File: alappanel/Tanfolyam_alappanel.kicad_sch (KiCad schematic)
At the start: 22 parts, among them J1 Connector, J2 Connector

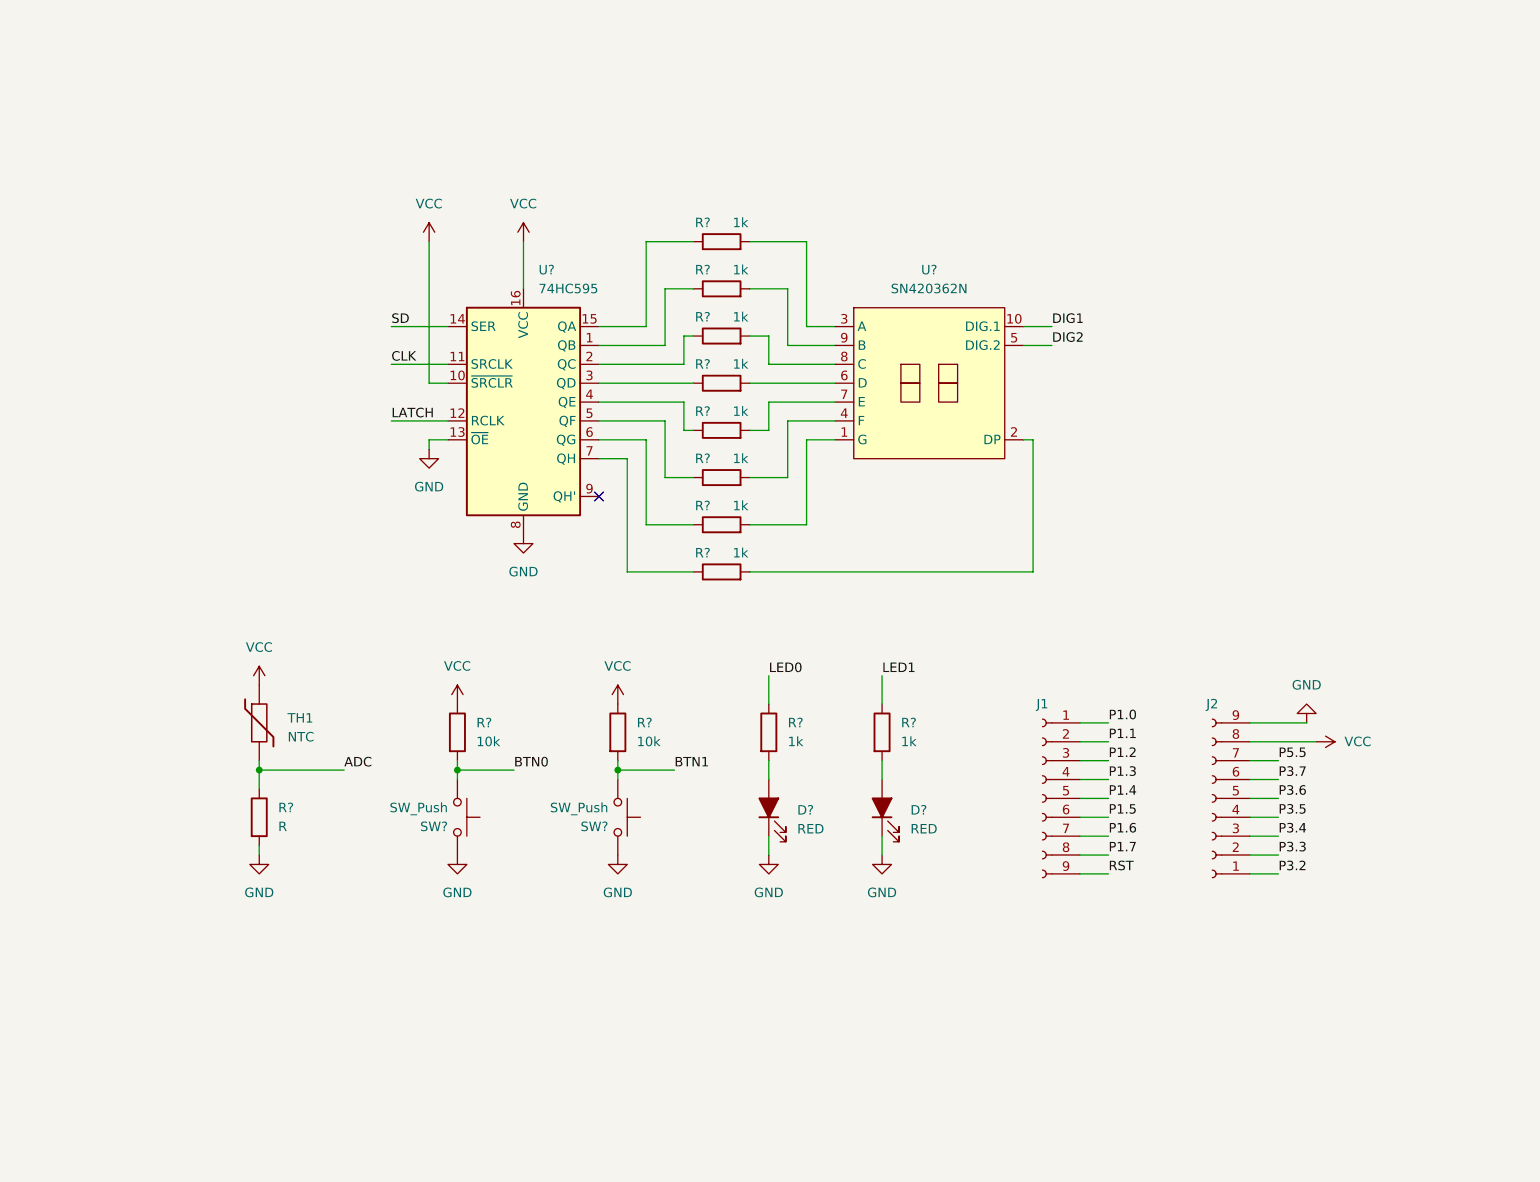
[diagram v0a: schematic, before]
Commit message: Add single sided base board
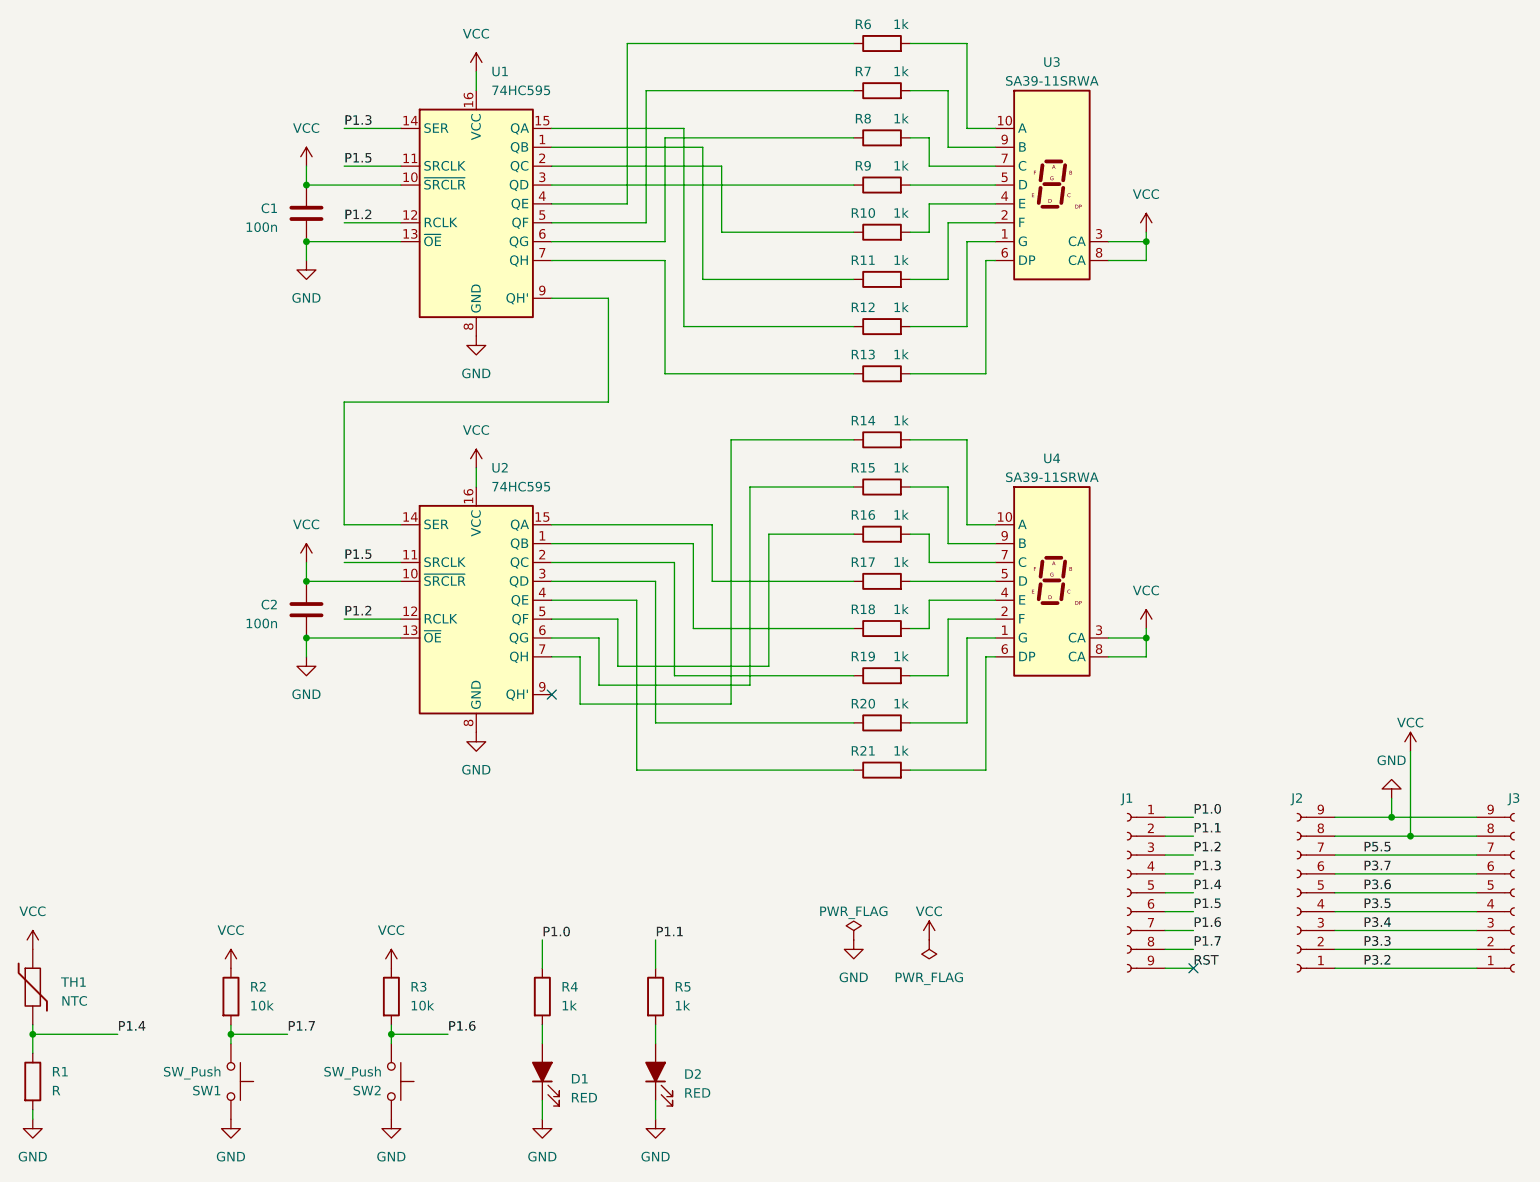
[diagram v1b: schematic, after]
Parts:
- removed R? (x7): 1k, symbol Device:R
- removed U?: SN420362N, sem-tanfolyam:SN420362N, symbol sem-tanfolyam:SN420362N
- removed U?: 74HC595, symbol 74xx:74HC595
- added C1, C2: 100n, Capacitor_SMD:C_0805_2012Metric_Pad1.18x1.45mm_HandSolder, symbol Device:C
- added J3: Connector, Connector_PinHeader_2.54mm:PinHeader_1x09_P2.54mm_Vertical, symbol Connector:Conn_01x09_Socket
- added R10, R11, R12, R13, R14, R15, R16, R17, R18, R19, R20, R21, R7, R8, R9: 1k, Resistor_SMD:R_0805_2012Metric_Pad1.20x1.40mm_HandSolder, symbol Device:R
- added U1, U2: 74HC595, Package_SO:SOIC-16_3.9x9.9mm_P1.27mm, symbol 74xx:74HC595
- added U3, U4: SA39-11SRWA, Display_7Segment:Sx39-1xxxxx, symbol Display_Character:SA39-11SRWA
- D1, D2: renamed from D?; footprint (none) -> LED_THT:LED_D5.0mm
- J1, J2: footprint (none) -> Connector_PinSocket_2.54mm:PinSocket_1x09_P2.54mm_Vertical
- R1, R2, R3, R4, R5, R6: renamed from R?; footprint (none) -> Resistor_SMD:R_0805_2012Metric_Pad1.20x1.40mm_HandSolder
- SW1, SW2: renamed from SW?; footprint (none) -> Button_Switch_THT:SW_PUSH_6mm
- TH1: footprint (none) -> Connector_PinHeader_2.54mm:PinHeader_1x02_P2.54mm_Vertical
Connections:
- net ADC is gone; now on net P1.4: R1.1, TH1.2
- net BTN0 is gone; now on net P1.7: R2.2, SW1.1
- net BTN1 is gone; now on net P1.6: R3.2, SW2.1
- net LED0 is gone; now on net P1.0: R4.1
- net LED1 is gone; now on net P1.1: R5.1
- net GND: now also C1.2, C2.2, J3.9 (Pin_9), U1.13 (~{OE}), U1.8 (GND), U2.13 (~{OE}), U2.8 (GND)
- net P1.2: now also U1.12 (RCLK), U2.12 (RCLK)
- net P1.3: now also U1.14 (SER)
- net P1.5: now also U1.11 (SRCLK), U2.11 (SRCLK)
- net P3.2: now also J3.1 (Pin_1)
- net P3.3: now also J3.2 (Pin_2)
- net P3.4: now also J3.3 (Pin_3)
- net P3.5: now also J3.4 (Pin_4)
- net P3.6: now also J3.5 (Pin_5)
- net P3.7: now also J3.6 (Pin_6)
- net P5.5: now also J3.7 (Pin_7)
- net VCC: now also C1.1, C2.1, J3.8 (Pin_8), U1.10 (~{SRCLR}), U1.16 (VCC), U2.10 (~{SRCLR}), U2.16 (VCC), U3.3 (CA), U3.8 (CA), U4.3 (CA), U4.8 (CA)
- net at R6.2: now also U3.10 (A)
- net at R6.1: now also U1.4 (QE)
- new net: R12.2, U3.1 (G)
- new net: R11.2, U3.2 (F)
- new net: R10.2, U3.4 (E)
- new net: R9.2, U3.5 (D)
- new net: R13.2, U3.6 (DP)
- new net: R8.2, U3.7 (C)
- new net: R7.2, U3.9 (B)
- new net: R20.2, U4.1 (G)
- new net: R14.2, U4.10 (A)
- new net: R19.2, U4.2 (F)
- new net: R18.2, U4.4 (E)
- new net: R17.2, U4.5 (D)
- new net: R21.2, U4.6 (DP)
- new net: R16.2, U4.7 (C)
- new net: R15.2, U4.9 (B)
- new net: R16.1, U2.5 (QF)
- new net: R12.1, U1.15 (QA)
- new net: R14.1, U2.7 (QH)
- new net: R8.1, U1.6 (QG)
- new net: R20.1, U2.3 (QD)
- new net: R21.1, U2.4 (QE)
- new net: R17.1, U2.15 (QA)
- new net: R19.1, U2.2 (QC)
- new net: R18.1, U2.1 (QB)
- new net: R11.1, U1.1 (QB)
- new net: R7.1, U1.5 (QF)
- new net: R10.1, U1.2 (QC)
- new net: R9.1, U1.3 (QD)
- new net: R13.1, U1.7 (QH)
- new net: U1.9 (QH'), U2.14 (SER)
- new net: R15.1, U2.6 (QG)
- no-connect marks 1 -> 2
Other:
- moved on the sheet: D1, D2, J1, J2, R1, R2, R3, R4, R5, R6, SW1, SW2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

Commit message: Changed 0805 footprints to 1206
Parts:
- C1, C2: footprint Capacitor_SMD:C_0805_2012Metric_Pad1.18x1.45mm_HandSolder -> Capacitor_SMD:C_1206_3216Metric_Pad1.33x1.80mm_HandSolder
- R1, R10, R11, R12, R13, R14, R15, R16, R17, R18, R19, R2, R20, R21, R3, R4, R5, R6, R7, R8, R9: footprint Resistor_SMD:R_0805_2012Metric_Pad1.20x1.40mm_HandSolder -> Resistor_SMD:R_1206_3216Metric_Pad1.30x1.75mm_HandSolder
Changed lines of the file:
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@@
       (effects (font (size 1.27 1.27)) (justify left))
     )
-    (property "Footprint" "Resistor_SMD:R_0805_2012Metric_Pad1.20x1.40mm_HandSolder" (at 78.232 158.75 90)
+    (property "Footprint" "Resistor_SMD:R_1206_3216Metric_Pad1.30x1.75mm_HandSolder" (at 78.232 158.75 90)
       (effects (font (size 1.27 1.27)) hide)
     )
@@
       (effects (font (size 1.27 1.27)))
     )
-    (property "Footprint" "Resistor_SMD:R_0805_2012Metric_Pad1.20x1.40mm_HandSolder" (at 167.64 98.298 90)
+    (property "Footprint" "Resistor_SMD:R_1206_3216Metric_Pad1.30x1.75mm_HandSolder" (at 167.64 98.298 90)
       (effects (font (size 1.27 1.27)) hide)
     )
@@
       (effects (font (size 1.27 1.27)))
     )
-    (property "Footprint" "Resistor_SMD:R_0805_2012Metric_Pad1.20x1.40mm_HandSolder" (at 167.64 70.358 90)
+    (property "Footprint" "Resistor_SMD:R_1206_3216Metric_Pad1.30x1.75mm_HandSolder" (at 167.64 70.358 90)
       (effects (font (size 1.27 1.27)) hide)
     )
@@
       (effects (font (size 1.27 1.27)))
     )
-    (property "Footprint" "Resistor_SMD:R_0805_2012Metric_Pad1.20x1.40mm_HandSolder" (at 167.64 85.598 90)
+    (property "Footprint" "Resistor_SMD:R_1206_3216Metric_Pad1.30x1.75mm_HandSolder" (at 167.64 85.598 90)
       (effects (font (size 1.27 1.27)) hide)
     )
@@
       (effects (font (size 1.27 1.27)))
     )
-    (property "Footprint" "Resistor_SMD:R_0805_2012Metric_Pad1.20x1.40mm_HandSolder" (at 167.64 44.958 90)
+    (property "Footprint" "Resistor_SMD:R_1206_3216Metric_Pad1.30x1.75mm_HandSolder" (at 167.64 44.958 90)
       (effects (font (size 1.27 1.27)) hide)
     )
@@
       (effects (font (size 1.27 1.27)))
     )
-    (property "Footprint" "Resistor_SMD:R_0805_2012Metric_Pad1.20x1.40mm_HandSolder" (at 167.64 123.698 90)
+    (property "Footprint" "Resistor_SMD:R_1206_3216Metric_Pad1.30x1.75mm_HandSolder" (at 167.64 123.698 90)
       (effects (font (size 1.27 1.27)) hide)
     )
@@
       (effects (font (size 1.27 1.27)) (justify left))
     )
-    (property "Footprint" "Resistor_SMD:R_0805_2012Metric_Pad1.20x1.40mm_HandSolder" (at 120.142 158.75 90)
+    (property "Footprint" "Resistor_SMD:R_1206_3216Metric_Pad1.30x1.75mm_HandSolder" (at 120.142 158.75 90)
       (effects (font (size 1.27 1.27)) hide)
     )
@@
       (effects (font (size 1.27 1.27)) (justify right))
     )
-    (property "Footprint" "Capacitor_SMD:C_0805_2012Metric_Pad1.18x1.45mm_HandSolder" (at 91.1352 57.15 0)
+    (property "Footprint" "Capacitor_SMD:C_1206_3216Metric_Pad1.33x1.80mm_HandSolder" (at 91.1352 57.15 0)
       (effects (font (size 1.27 1.27)) hide)
     )
@@
       (effects (font (size 1.27 1.27)) (justify left))
     )
-    (property "Footprint" "Resistor_SMD:R_0805_2012Metric_Pad1.20x1.40mm_HandSolder" (at 99.822 158.75 90)
+    (property "Footprint" "Resistor_SMD:R_1206_3216Metric_Pad1.30x1.75mm_HandSolder" (at 99.822 158.75 90)
       (effects (font (size 1.27 1.27)) hide)
     )
@@
       (effects (font (size 1.27 1.27)))
     )
-    (property "Footprint" "Resistor_SMD:R_0805_2012Metric_Pad1.20x1.40mm_HandSolder" (at 167.64 130.048 90)
+    (property "Footprint" "Resistor_SMD:R_1206_3216Metric_Pad1.30x1.75mm_HandSolder" (at 167.64 130.048 90)
       (effects (font (size 1.27 1.27)) hide)
     )
@@
       (effects (font (size 1.27 1.27)))
     )
-    (property "Footprint" "Resistor_SMD:R_0805_2012Metric_Pad1.20x1.40mm_HandSolder" (at 167.64 104.648 90)
+    (property "Footprint" "Resistor_SMD:R_1206_3216Metric_Pad1.30x1.75mm_HandSolder" (at 167.64 104.648 90)
       (effects (font (size 1.27 1.27)) hide)
     )
@@
       (effects (font (size 1.27 1.27)))
     )
-    (property "Footprint" "Resistor_SMD:R_0805_2012Metric_Pad1.20x1.40mm_HandSolder" (at 167.64 117.348 90)
+    (property "Footprint" "Resistor_SMD:R_1206_3216Metric_Pad1.30x1.75mm_HandSolder" (at 167.64 117.348 90)
       (effects (font (size 1.27 1.27)) hide)
     )
@@
       (effects (font (size 1.27 1.27)))
     )
-    (property "Footprint" "Resistor_SMD:R_0805_2012Metric_Pad1.20x1.40mm_HandSolder" (at 167.64 110.998 90)
+    (property "Footprint" "Resistor_SMD:R_1206_3216Metric_Pad1.30x1.75mm_HandSolder" (at 167.64 110.998 90)
       (effects (font (size 1.27 1.27)) hide)
     )
@@
       (effects (font (size 1.27 1.27)))
     )
-    (property "Footprint" "Resistor_SMD:R_0805_2012Metric_Pad1.20x1.40mm_HandSolder" (at 167.64 64.008 90)
+    (property "Footprint" "Resistor_SMD:R_1206_3216Metric_Pad1.30x1.75mm_HandSolder" (at 167.64 64.008 90)
       (effects (font (size 1.27 1.27)) hide)
     )
@@
       (effects (font (size 1.27 1.27)))
     )
-    (property "Footprint" "Resistor_SMD:R_0805_2012Metric_Pad1.20x1.40mm_HandSolder" (at 167.64 38.608 90)
+    (property "Footprint" "Resistor_SMD:R_1206_3216Metric_Pad1.30x1.75mm_HandSolder" (at 167.64 38.608 90)
       (effects (font (size 1.27 1.27)) hide)
     )
@@
       (effects (font (size 1.27 1.27)))
     )
-    (property "Footprint" "Resistor_SMD:R_0805_2012Metric_Pad1.20x1.40mm_HandSolder" (at 167.64 57.658 90)
+    (property "Footprint" "Resistor_SMD:R_1206_3216Metric_Pad1.30x1.75mm_HandSolder" (at 167.64 57.658 90)
       (effects (font (size 1.27 1.27)) hide)
     )
@@
       (effects (font (size 1.27 1.27)))
     )
-    (property "Footprint" "Resistor_SMD:R_0805_2012Metric_Pad1.20x1.40mm_HandSolder" (at 167.64 91.948 90)
+    (property "Footprint" "Resistor_SMD:R_1206_3216Metric_Pad1.30x1.75mm_HandSolder" (at 167.64 91.948 90)
       (effects (font (size 1.27 1.27)) hide)
     )
@@
       (effects (font (size 1.27 1.27)) (justify right))
     )
-    (property "Footprint" "Capacitor_SMD:C_0805_2012Metric_Pad1.18x1.45mm_HandSolder" (at 91.1352 110.49 0)
+    (property "Footprint" "Capacitor_SMD:C_1206_3216Metric_Pad1.33x1.80mm_HandSolder" (at 91.1352 110.49 0)
       (effects (font (size 1.27 1.27)) hide)
     )
@@
       (effects (font (size 1.27 1.27)))
     )
-    (property "Footprint" "Resistor_SMD:R_0805_2012Metric_Pad1.20x1.40mm_HandSolder" (at 167.64 76.708 90)
+    (property "Footprint" "Resistor_SMD:R_1206_3216Metric_Pad1.30x1.75mm_HandSolder" (at 167.64 76.708 90)
       (effects (font (size 1.27 1.27)) hide)
     )
@@
       (effects (font (size 1.27 1.27)))
     )
-    (property "Footprint" "Resistor_SMD:R_0805_2012Metric_Pad1.20x1.40mm_HandSolder" (at 167.64 32.258 90)
+    (property "Footprint" "Resistor_SMD:R_1206_3216Metric_Pad1.30x1.75mm_HandSolder" (at 167.64 32.258 90)
       (effects (font (size 1.27 1.27)) hide)
     )
@@
       (effects (font (size 1.27 1.27)))
     )
-    (property "Footprint" "Resistor_SMD:R_0805_2012Metric_Pad1.20x1.40mm_HandSolder" (at 167.64 51.308 90)
+    (property "Footprint" "Resistor_SMD:R_1206_3216Metric_Pad1.30x1.75mm_HandSolder" (at 167.64 51.308 90)
       (effects (font (size 1.27 1.27)) hide)
     )
@@
       (effects (font (size 1.27 1.27)) (justify left))
     )
-    (property "Footprint" "Resistor_SMD:R_0805_2012Metric_Pad1.20x1.40mm_HandSolder" (at 135.382 158.75 90)
+    (property "Footprint" "Resistor_SMD:R_1206_3216Metric_Pad1.30x1.75mm_HandSolder" (at 135.382 158.75 90)
       (effects (font (size 1.27 1.27)) hide)
     )
@@
       (effects (font (size 1.27 1.27)) (justify left))
     )
-    (property "Footprint" "Resistor_SMD:R_0805_2012Metric_Pad1.20x1.40mm_HandSolder" (at 51.562 170.18 90)
-      (effects (font (size 1.27 1.27)) hide)
-    )
+    (property "Footprint" "Resistor_SMD:R_1206_3216Metric_Pad1.30x1.75mm_HandSolder" (at 51.562 170.18 90)
+      (effects (font (size 1.27 1.27)) hide)
+    )

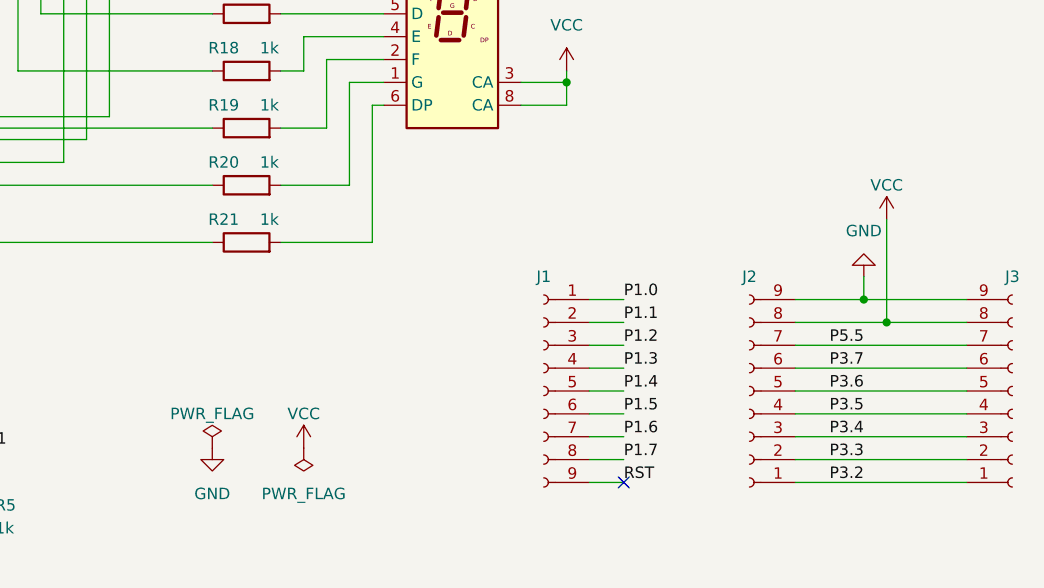
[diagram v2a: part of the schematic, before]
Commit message: Add 7-segment display 3D model and tutorial (demo) project for kicad8
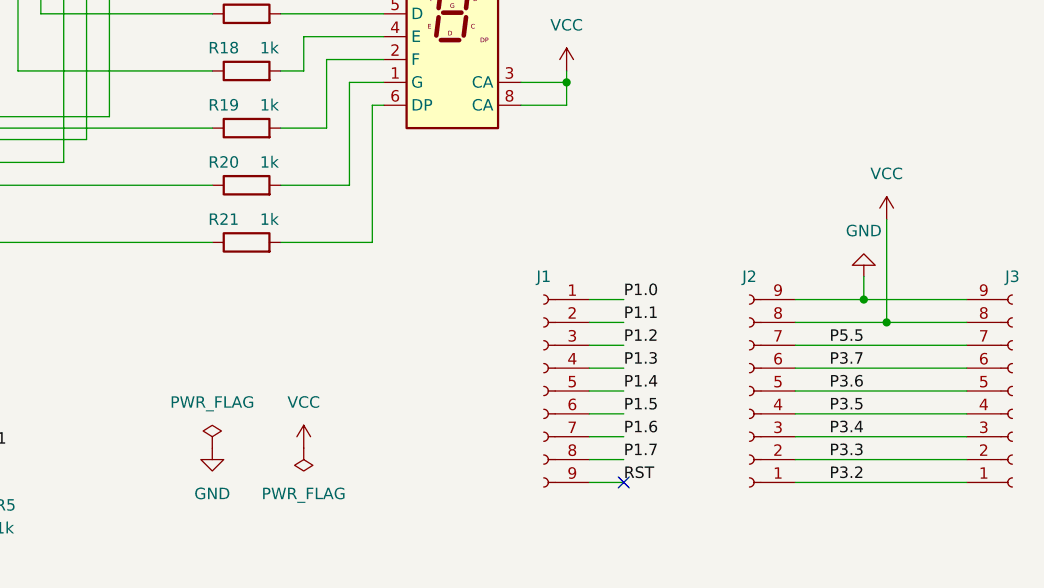
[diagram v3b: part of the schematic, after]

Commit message: Demo projekt
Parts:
- R1: value R -> 10k
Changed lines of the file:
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@@
 			)
 		)
-		(property "Value" "R"
+		(property "Value" "10k"
 			(at 55.88 171.4499 0)
 			(effects
